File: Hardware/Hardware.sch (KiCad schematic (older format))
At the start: 21 parts

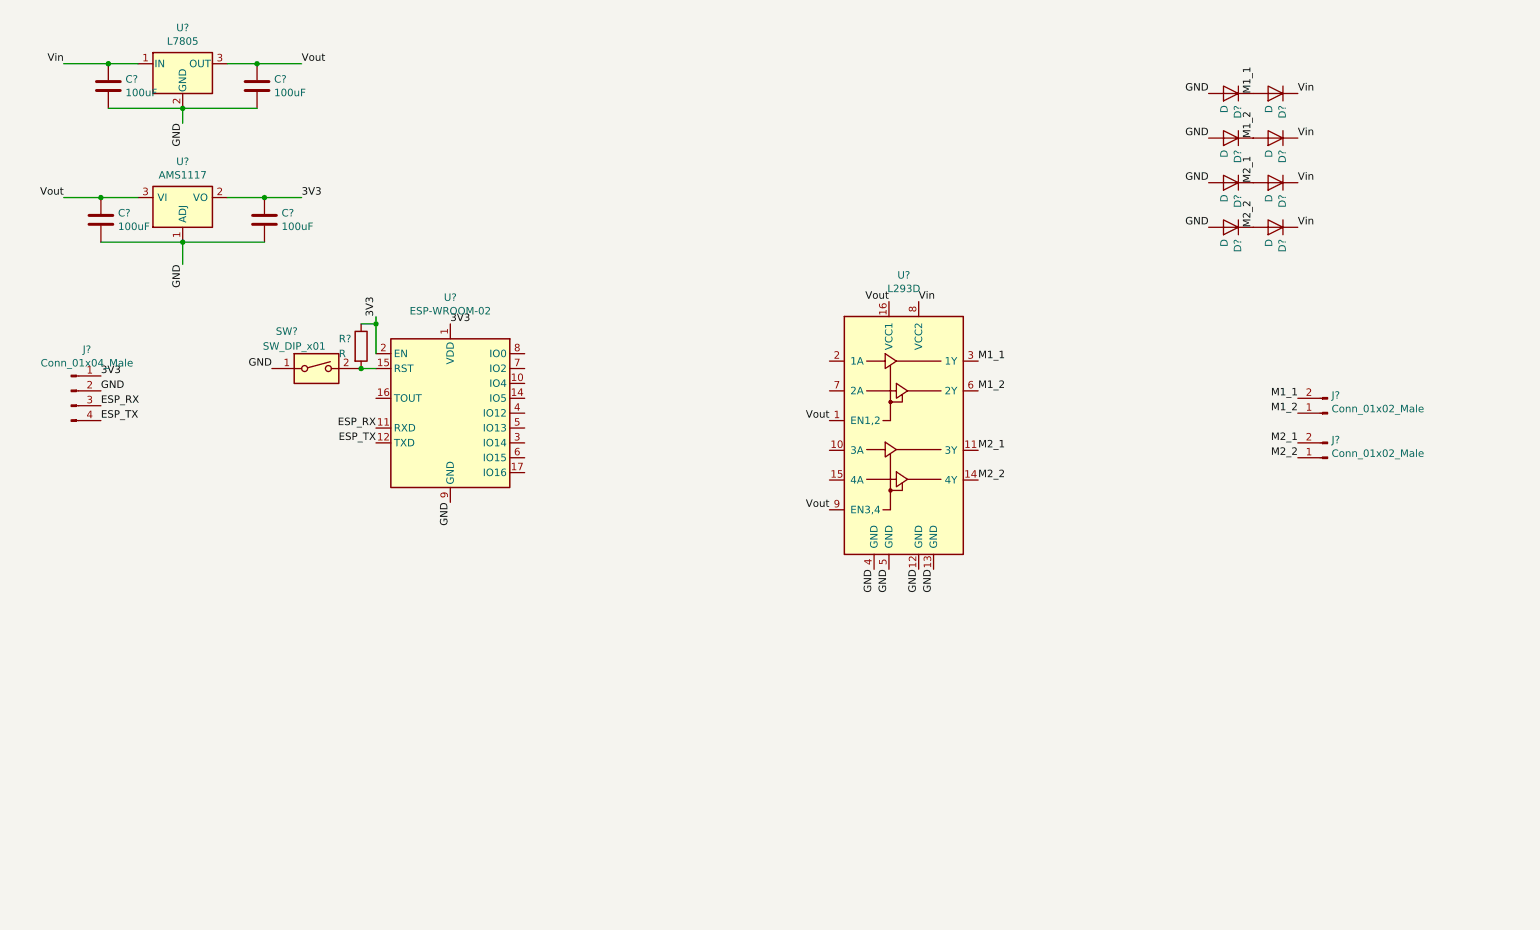
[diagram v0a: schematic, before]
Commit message: Added motor driver, MCU, radio
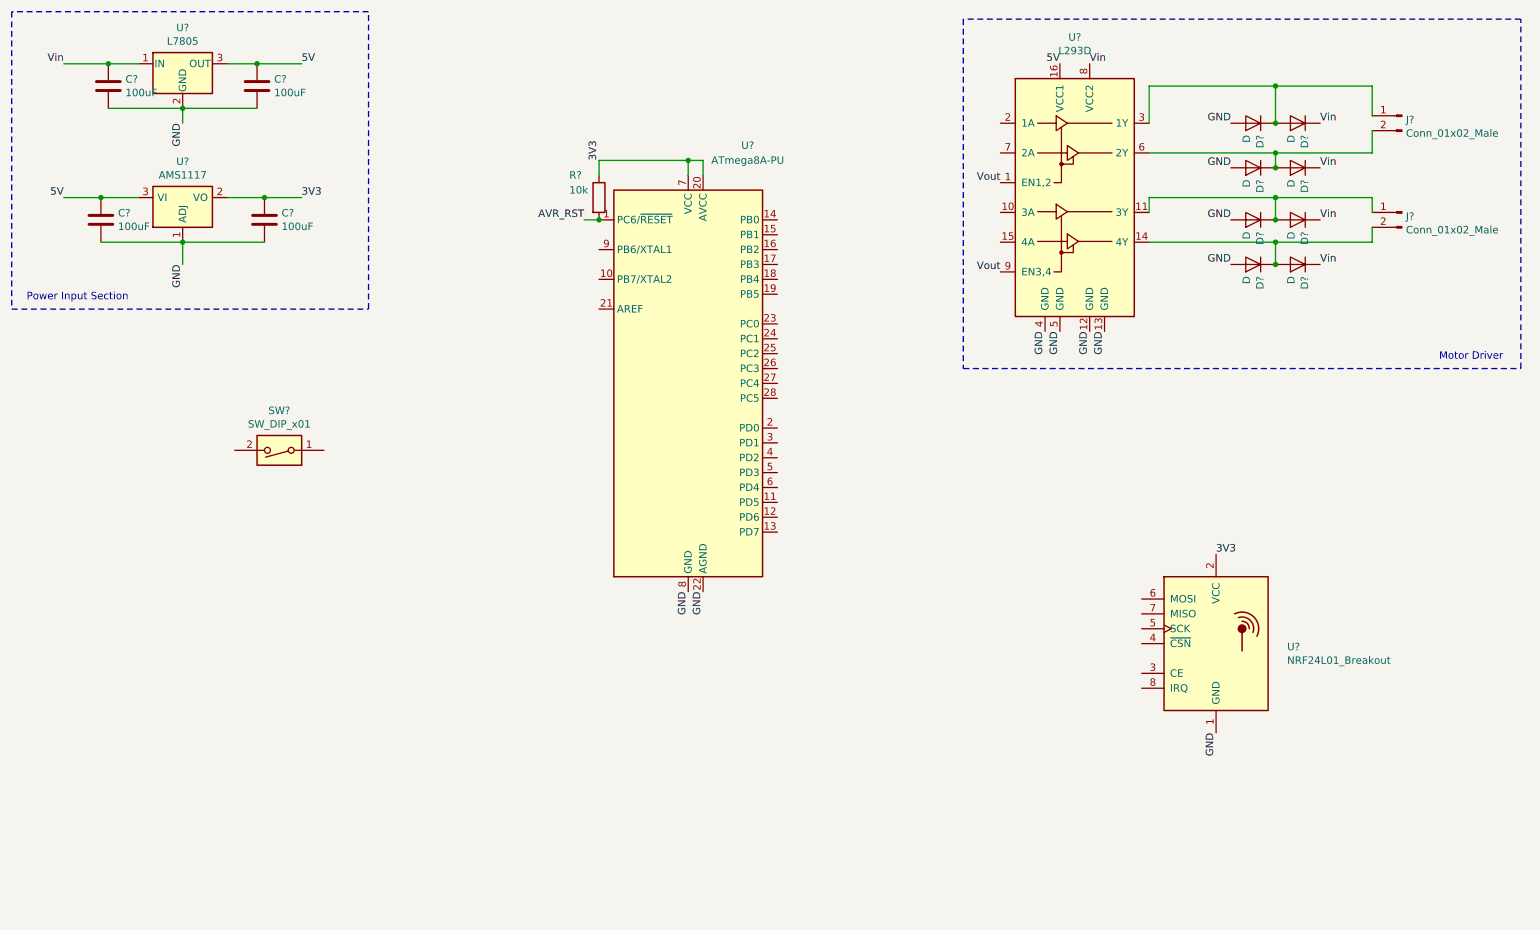
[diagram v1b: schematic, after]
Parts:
- removed J?: Conn_01x04_Male, symbol Connector:Conn_01x04_Male
- removed R?: R, symbol Device:R
- removed SW?: SW_DIP_x01, symbol Switch:SW_DIP_x01
- removed U?: ESP-WROOM-02, RF_Module:ESP-WROOM-02, symbol RF_Module:ESP-WROOM-02
- added R?: 10k, symbol Device:R
- added SW?: SW_DIP_x01, symbol Switch:SW_DIP_x01
- added U?: NRF24L01_Breakout, RF_Module:nRF24L01_Breakout, symbol RF:NRF24L01_Breakout
- added U?: ATmega8A-PU, Package_DIP:DIP-28_W7.62mm, symbol MCU_Microchip_ATmega:ATmega8A-PU
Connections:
- net 3V3: now also R?.1, U?.2 (VCC), U?.20 (AVCC), U?.7 (VCC)
- net GND: now also U?.1 (GND), U?.22 (AGND), U?.8 (GND)
- net Vout: no longer C?.2, C?.2, U?.16 (VCC1), U?.3 (OUT), U?.3 (VI)
- net M1_1: no longer names the net of D?.1 (K), D?.2 (A), U?.3 (1Y)
- net M1_1: now also J?.1 (Pin_1); no longer J?.2 (Pin_2)
- net M1_2: no longer names the net of D?.1 (K), D?.2 (A), U?.6 (2Y)
- net M1_2: now also J?.2 (Pin_2); no longer J?.1 (Pin_1)
- net M2_1: no longer names the net of D?.1 (K), D?.2 (A), U?.11 (3Y)
- net M2_1: now also J?.1 (Pin_1); no longer J?.2 (Pin_2)
- net M2_2: no longer names the net of D?.1 (K), D?.2 (A), U?.14 (4Y)
- net M2_2: now also J?.2 (Pin_2); no longer J?.1 (Pin_1)
- new net 5V: C?.2, C?.2, U?.16 (VCC1), U?.3 (OUT), U?.3 (VI)
- new net AVR_RST: R?.2, U?.1 (PC6/~RESET)
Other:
- note added: "Motor Driver"
- note added: "Power Input Section"
- moved on the sheet: D?, J?, U?

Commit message: Added RF chip
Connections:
- net 3V3: now also U?.3 (CE)
- net NRF_CHSEL: now reaches U?.4 (~CSN)
- net NRF_CHSEL: now also U?.14 (PB0)
- net SCK: now reaches U?.5 (SCK)
- net SCK: now also U?.19 (PB5)
- net MOSI: now reaches U?.6 (MOSI)
- net MOSI: now also U?.17 (PB3)
- net MISO: now reaches U?.7 (MISO)
- net MISO: now also U?.18 (PB4)
- net INTERRUPT: now reaches U?.8 (IRQ)
- net INTERRUPT: now also U?.4 (PD2)
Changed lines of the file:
@@
 EESchema Schematic File Version 4
+LIBS:Hardware-cache
 EELAYER 26 0
 EELAYER END
@@
 Text Label 5600 4450 3    50   ~ 0
 GND
+Text Label 6100 2450 0    50   ~ 0
+SCK
+Text Label 6100 2350 0    50   ~ 0
+MISO
+Text Label 6100 2250 0    50   ~ 0
+MOSI
+Text Label 8550 5100 2    50   ~ 0
+INTERRUPT
+Text Label 6100 3550 0    50   ~ 0
+INTERRUPT
+Text Label 8550 4700 2    50   ~ 0
+SCK
+Text Label 8550 4600 2    50   ~ 0
+MISO
+Text Label 8550 4500 2    50   ~ 0
+MOSI
+Text Label 6100 1950 0    50   ~ 0
+NRF_CHSEL
+Text Label 8550 4800 2    50   ~ 0
+NRF_CHSEL
+Text Label 8550 5000 2    50   ~ 0
+3V3
 $EndSCHEMATC

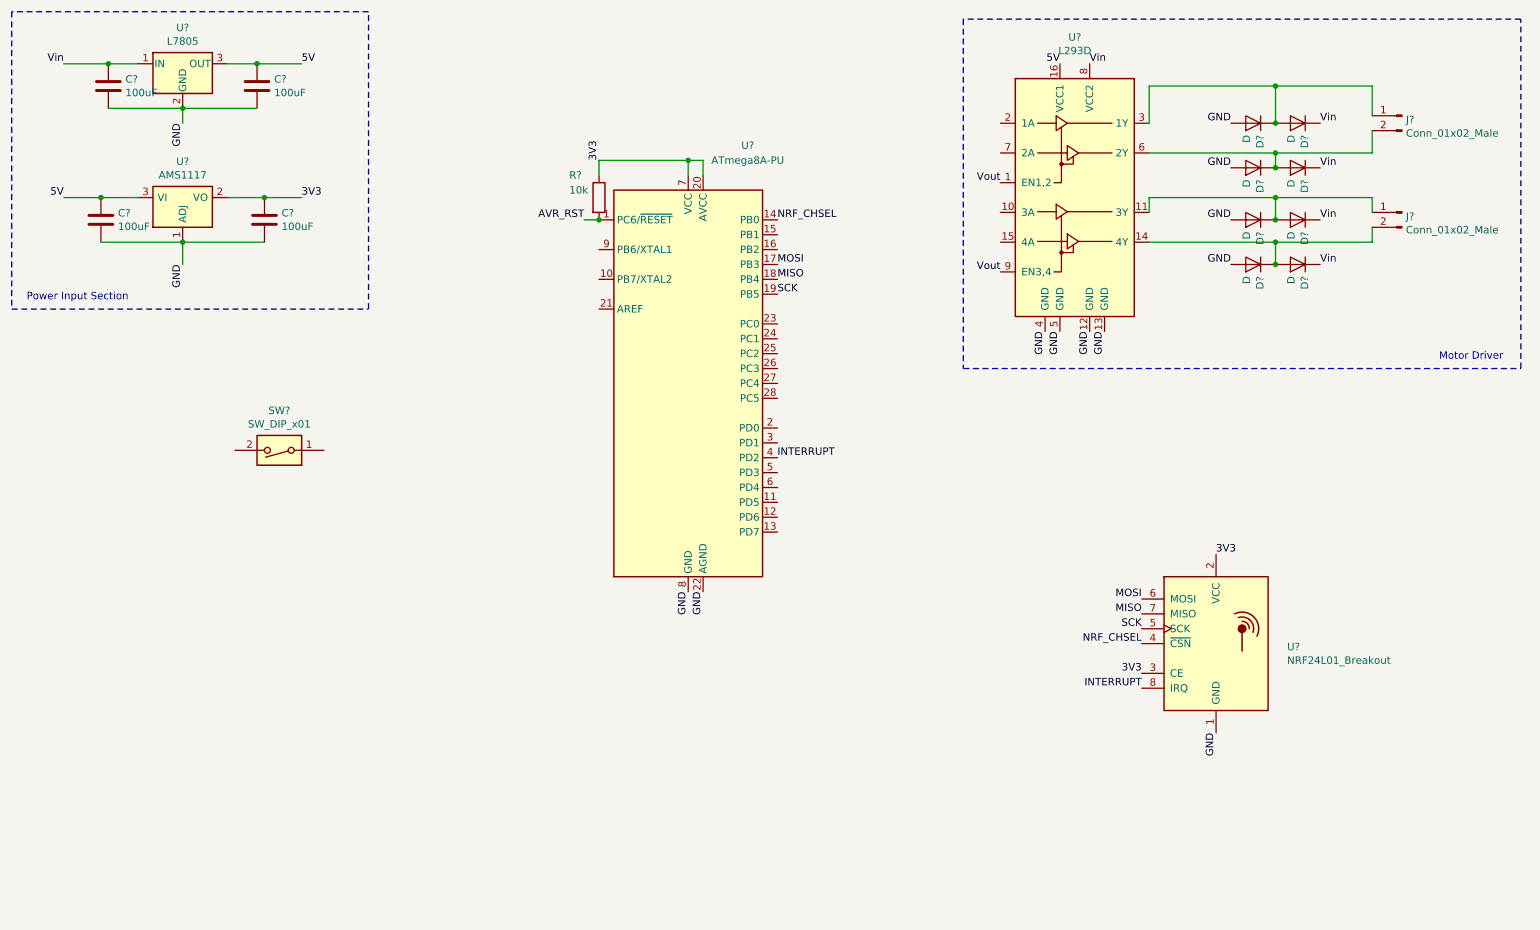
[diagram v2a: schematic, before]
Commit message: Added LEDs
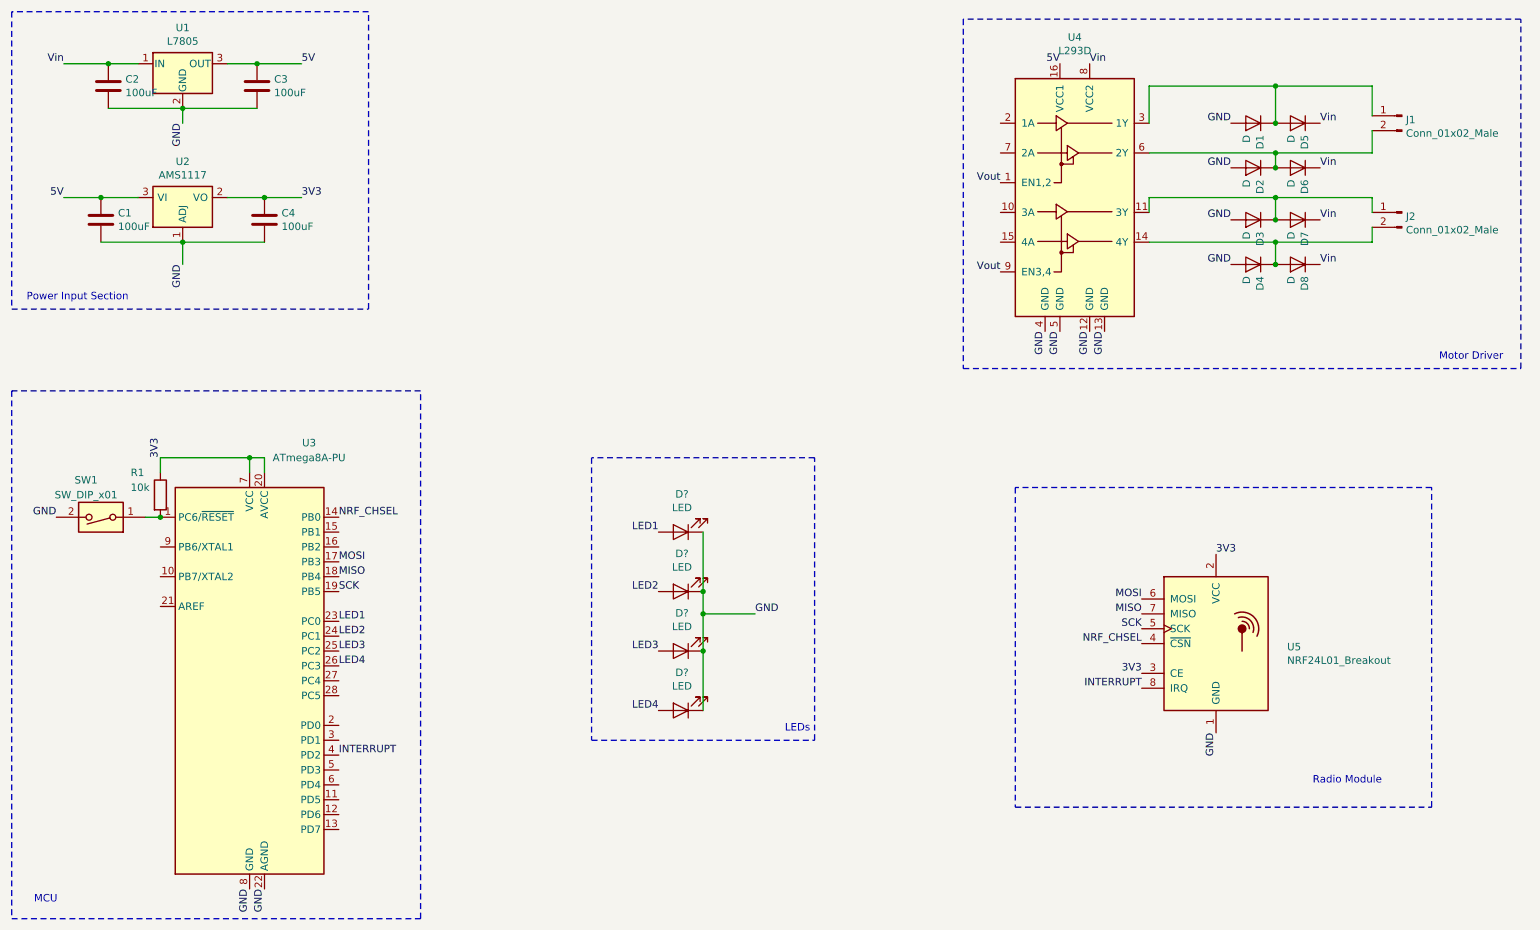
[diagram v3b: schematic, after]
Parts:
- added D? (x4): LED, symbol Device:LED
- C1, C2, C3, C4: renamed from C?; footprint (none) -> Capacitor_THT:CP_Radial_D6.3mm_P2.50mm
- D1, D2, D3, D4, D5, D6, D7, D8: renamed from D?; footprint (none) -> Diode_THT:D_DO-15_P10.16mm_Horizontal
- J1, J2: renamed from J?; footprint (none) -> Connector_PinSocket_2.54mm:PinSocket_1x02_P2.54mm_Vertical
- R1: renamed from R?; footprint (none) -> Resistor_THT:R_Axial_DIN0204_L3.6mm_D1.6mm_P1.90mm_Vertical
- SW1: renamed from SW?; footprint (none) -> Button_Switch_THT:SW_PUSH_6mm_H5mm
- gave numbers to parts that had none: 5
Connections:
- net AVR_RST is gone; now on an unnamed net: R1.2, U3.1 (PC6/~RESET)
- net GND: now also SW1.2, D?.1 (K), D?.1 (K), D?.1 (K), D?.1 (K)
- net LED1: now reaches U3.23 (PC0)
- net LED1: now also D?.2 (A)
- net LED2: now reaches U3.24 (PC1)
- net LED2: now also D?.2 (A)
- net LED3: now reaches U3.25 (PC2)
- net LED3: now also D?.2 (A)
- net LED4: now reaches U3.26 (PC3)
- net LED4: now also D?.2 (A)
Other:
- note added: "LEDs"
- note added: "MCU"
- note added: "Radio Module"
- moved on the sheet: R1, SW1, U3

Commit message: Added netlist
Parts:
- D10, D11, D12, D9: renamed from D?; footprint (none) -> Diode_SMD:D_0603_1608Metric_Pad1.05x0.95mm_HandSolder
- U1: footprint (none) -> Package_TO_SOT_THT:TO-220F-3_Vertical
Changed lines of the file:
@@
 F 0 "U1" H 2100 1142 50  0000 C CNN
 F 1 "L7805" H 2100 1051 50  0000 C CNN
-F 2 "" H 2125 750 50  0001 L CIN
+F 2 "Package_TO_SOT_THT:TO-220F-3_Vertical" H 2125 750 50  0001 L CIN
 F 3 "http://www.st.com/content/ccc/resource/technical/document/datasheet/41/4f/b3/b0/12/d4/47/88/CD00000444.pdf/files/CD00000444.pdf/jcr:content/translations/en.CD00000444.pdf" H 2100 850 50  0001 C CNN
 	1    2100 900
@@
 Radio Module
 $Comp
-L Device:LED D?
+L Device:LED D9
 U 1 1 5F47FBAF
 P 5450 4050
-F 0 "D?" H 5442 3795 50  0000 C CNN
+F 0 "D9" H 5442 3795 50  0000 C CNN
 F 1 "LED" H 5442 3886 50  0000 C CNN
-F 2 "" H 5450 4050 50  0001 C CNN
+F 2 "Diode_SMD:D_0603_1608Metric_Pad1.05x0.95mm_HandSolder" H 5450 4050 50  0001 C CNN
 F 3 "~" H 5450 4050 50  0001 C CNN
 	1    5450 4050
@@
 $EndComp
 $Comp
-L Device:LED D?
+L Device:LED D10
 U 1 1 5F47FEF5
 P 5450 4450
-F 0 "D?" H 5442 4195 50  0000 C CNN
+F 0 "D10" H 5442 4195 50  0000 C CNN
 F 1 "LED" H 5442 4286 50  0000 C CNN
-F 2 "" H 5450 4450 50  0001 C CNN
+F 2 "Diode_SMD:D_0603_1608Metric_Pad1.05x0.95mm_HandSolder" H 5450 4450 50  0001 C CNN
 F 3 "~" H 5450 4450 50  0001 C CNN
 	1    5450 4450
@@
 $EndComp
 $Comp
-L Device:LED D?
+L Device:LED D11
 U 1 1 5F47FF3F
 P 5450 4850
-F 0 "D?" H 5442 4595 50  0000 C CNN
+F 0 "D11" H 5442 4595 50  0000 C CNN
 F 1 "LED" H 5442 4686 50  0000 C CNN
-F 2 "" H 5450 4850 50  0001 C CNN
+F 2 "Diode_SMD:D_0603_1608Metric_Pad1.05x0.95mm_HandSolder" H 5450 4850 50  0001 C CNN
 F 3 "~" H 5450 4850 50  0001 C CNN
 	1    5450 4850
@@
 $EndComp
 $Comp
-L Device:LED D?
+L Device:LED D12
 U 1 1 5F47FF8B
 P 5450 5250
-F 0 "D?" H 5442 4995 50  0000 C CNN
+F 0 "D12" H 5442 4995 50  0000 C CNN
 F 1 "LED" H 5442 5086 50  0000 C CNN
-F 2 "" H 5450 5250 50  0001 C CNN
+F 2 "Diode_SMD:D_0603_1608Metric_Pad1.05x0.95mm_HandSolder" H 5450 5250 50  0001 C CNN
 F 3 "~" H 5450 5250 50  0001 C CNN
 	1    5450 5250

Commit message: Added PCB design
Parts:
- added J3: Conn_01x02_Male, Connector_PinSocket_2.54mm:PinSocket_1x02_P2.54mm_Vertical, symbol Connector:Conn_01x02_Male
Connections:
- net GND: now also J3.2 (Pin_2)
- net Vin: now also J3.1 (Pin_1)
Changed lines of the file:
@@
 Text Notes 6150 5400 0    50   ~ 0
 LEDs
+$Comp
+L Connector:Conn_01x02_Male J3
+U 1 1 5F4D87DB
+P 5200 2200
+F 0 "J3" H 5306 2378 50  0000 C CNN
+F 1 "Conn_01x02_Male" H 5306 2287 50  0000 C CNN
+F 2 "Connector_PinSocket_2.54mm:PinSocket_1x02_P2.54mm_Vertical" H 5200 2200 50  0001 C CNN
+F 3 "~" H 5200 2200 50  0001 C CNN
+	1    5200 2200
+	1    0    0    -1
+$EndComp
+Text Label 5400 2200 0    50   ~ 0
+Vin
+Text Label 5400 2300 0    50   ~ 0
+GND
 $EndSCHEMATC
